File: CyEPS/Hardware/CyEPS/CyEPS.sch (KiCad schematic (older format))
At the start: 98 parts

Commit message: Board fully routed for the first time
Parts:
- removed J?: Conn_01x05_Female, symbol Connector:Conn_01x05_Female
- added J1, J2: Conn_01x04_Female, Connector_Molex:Molex_Micro-Fit_3.0_43650-0400_1x04_P3.00mm_Horizontal, symbol Connector:Conn_01x04_Female
- Batt_1: footprint (none) -> Connector_Wire:SolderWire-0.127sqmm_1x02_P3.7mm_D0.48mm_OD1mm
- Batt_2, Batt_3: footprint (none) -> Connector_JST:JST_PH_S2B-PH-K_1x02_P2.00mm_Horizontal
- C1, C2, C21, C22, C24, C25, C3, C4, C6: renamed from C?; footprint (none) -> Capacitor_THT:CP_Radial_Tantal_D5.0mm_P2.50mm
- C10, C11, C12, C13, C14, C15, C16, C17, C18, C19, C20, C23, C26, C27, C28, C29, C5, C7, C8, C9: renamed from C?; footprint (none) -> Capacitor_SMD:C_0805_2012Metric_Pad1.18x1.45mm_HandSolder
- C30: renamed from C?; value CP1 -> 2200uF; footprint (none) -> Capacitor_THT:CP_Radial_Tantal_D5.0mm_P2.50mm
- D1, D2, D5: renamed from D?; footprint (none) -> Diode_SMD:D_SOD-523
- D3, D4, D6: renamed from D?; footprint (none) -> LED_THT:LED_D5.0mm
- L1, L2: renamed from L?; footprint (none) -> Inductor_SMD:L_0805_2012Metric_Pad1.15x1.40mm_HandSolder
- R1, R10, R11, R12, R13, R14, R15, R16, R17, R18, R19, R2, R20, R21, R22, R23, R24, R25, R26, R27, R3, R4, R5, R6, R7, R8, R9: renamed from R?; footprint (none) -> Resistor_SMD:R_0815_2038Metric_Pad1.20x4.05mm_HandSolder
- R28, R40: renamed from R?; footprint (none) -> Resistor_SMD:R_Shunt_Ohmite_LVK12
- R29, R30, R31, R32, R33, R34, R35, R36, R37, R38, R39, R41: renamed from R?; footprint (none) -> Resistor_SMD:R_0805_2012Metric_Pad1.20x1.40mm_HandSolder
- U4: renamed from U?; footprint MTC16 -> footprints:ADC128D818CIMTX&slash_NOPB
- U5, U6: renamed from U?; footprint (none) -> Package_TO_SOT_SMD:SOT-223
- gave numbers to parts that had none: 9
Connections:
- net GND: now also C13.2, C14.2, C15.2, C16.2, C18.2, C19.2, J1.3 (Pin_3), J2.3 (Pin_3)
- net Payload3V3: now also J2.2 (Pin_2)
- net Payload5V: now also J2.1 (Pin_1)
- net PayloadEnable: now also J1.4 (Pin_4)
- net Primary3V3: now also J1.2 (Pin_2)
- net Primary5V: now also J1.1 (Pin_1)
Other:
- moved on the sheet: R41

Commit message: Power traces redone in .4mm width (max that would fit voltage select chip pads)
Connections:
- net GND: now also U3.13 (GND)
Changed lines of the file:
@@
 Wire Wire Line
 	9700 2400 9700 2350
+$Comp
+L power:GND #PWR?
+U 1 1 604A121E
+P 3900 5100
+F 0 "#PWR?" H 3900 4850 50  0001 C CNN
+F 1 "GND" H 3905 4927 50  0000 C CNN
+F 2 "" H 3900 5100 50  0001 C CNN
+F 3 "" H 3900 5100 50  0001 C CNN
+	1    3900 5100
+	1    0    0    -1
+$EndComp
 $EndSCHEMATC

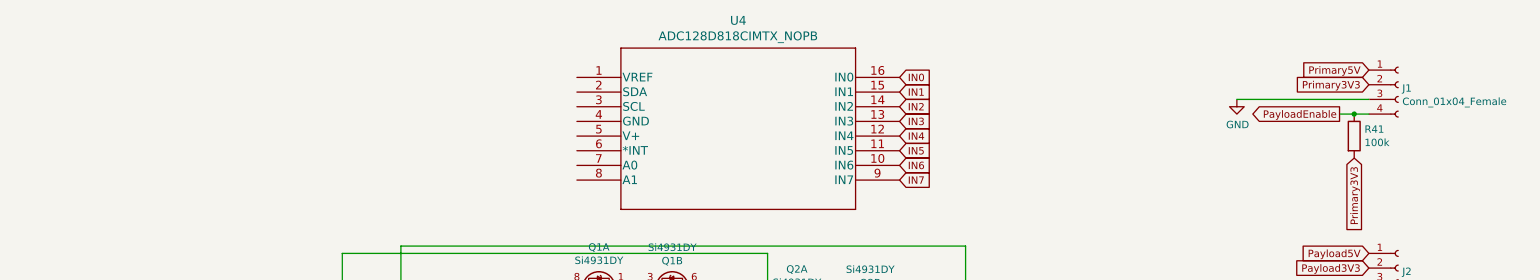
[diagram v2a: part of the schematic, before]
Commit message: form factor changed to 10cm x 10cm among other changes after review
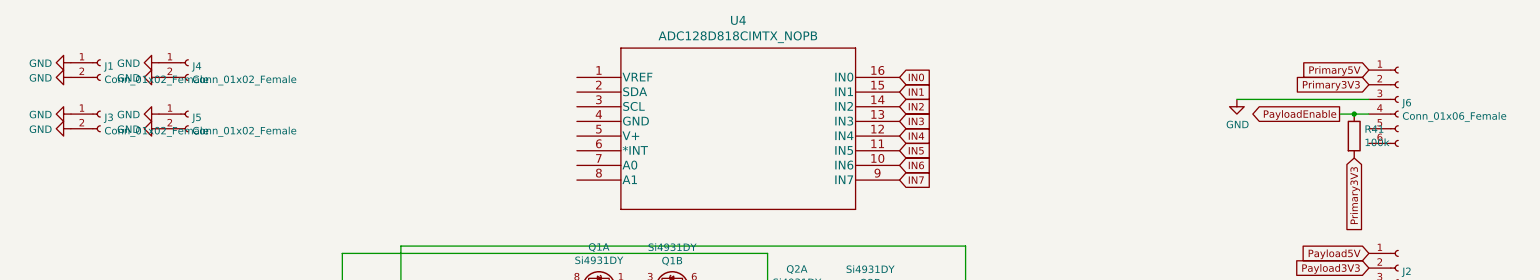
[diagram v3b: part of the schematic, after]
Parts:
- removed J1: Conn_01x04_Female, Connector_Molex:Molex_Micro-Fit_3.0_43650-0400_1x04_P3.00mm_Horizontal, symbol Connector:Conn_01x04_Female
- added J1, J3, J4, J5: Conn_01x02_Female, Connector_PinHeader_2.54mm:PinHeader_1x02_P2.54mm_Vertical, symbol Connector:Conn_01x02_Female
- added J6: Conn_01x06_Female, Connector_PinHeader_2.54mm:PinHeader_1x06_P2.54mm_Vertical, symbol Connector:Conn_01x06_Female
- C1, C2, C21, C22, C24, C25, C3, C30, C4, C6: footprint Capacitor_THT:CP_Radial_Tantal_D5.0mm_P2.50mm -> Capacitor_Tantalum_SMD:CP_EIA-1608-08_AVX-J_Pad1.25x1.05mm_HandSolder
- D3, D4, D6: footprint LED_THT:LED_D5.0mm -> LED_SMD:LED_0805_2012Metric_Pad1.15x1.40mm_HandSolder
- R1, R10, R11, R12, R13, R14, R15, R16, R17, R18, R19, R2, R20, R21, R22, R23, R24, R25, R26, R27, R3, R4, R5, R6, R7, R8, R9: footprint Resistor_SMD:R_0815_2038Metric_Pad1.20x4.05mm_HandSolder -> Resistor_SMD:R_0805_2012Metric_Pad1.20x1.40mm_HandSolder
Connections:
- net GND: now also J1.1 (Pin_1), J1.2 (Pin_2), J3.1 (Pin_1), J3.2 (Pin_2), J4.1 (Pin_1), J4.2 (Pin_2), J5.1 (Pin_1), J5.2 (Pin_2), J6.3 (Pin_3)
- net PayloadEnable: now also J6.4 (Pin_4)
- net Primary3V3: now also J6.2 (Pin_2)
- net Primary5V: now also J6.1 (Pin_1)
